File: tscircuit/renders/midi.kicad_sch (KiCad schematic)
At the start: 8 parts, among them U6 H11L1

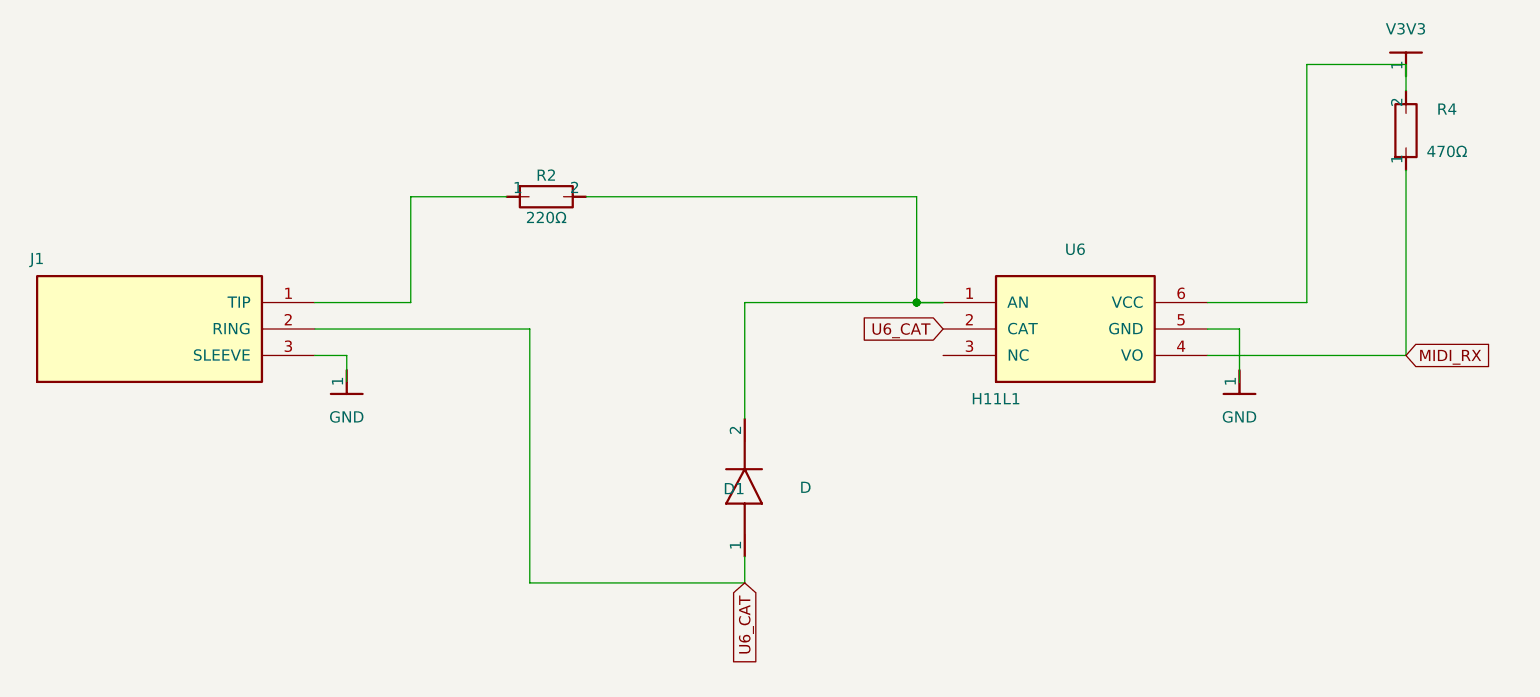
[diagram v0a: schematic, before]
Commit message: tscircuit: full-board schematic-as-code (MIDI + USB + MCU)
Recreate the entire OpenRB rev 0.2 board as tscircuit code from RECONSTRUCTION.md,
using the exact LCSC parts (imported with EasyEDA footprints). Three sheets joined
by shared net-label names; each renders a schematic and exports a native .kicad_sch
that kicad-cli re-opens.

- midi.tsx (§5): DIN-5 MIDI IN -> H11L1 opto (fully hand-wired).
- usb.tsx (§4): USB-C + USBLC6 ESD + CH334R hub + dual USB-A + bulk caps.
- mcu.tsx (§3/§6): RP2040 + power (F1/RT9080) + QSPI flash + 12MHz + reset/boot +
  SWD/UART headers + status LEDs + decoupling.

Independently verified connection-by-connection against RECONSTRUCTION §3-6: all
pass. Fixed one error found in review: C10/C11 100nF moved from +3V3 to the 1.1V
core rail (V1V1) per §2. MIDI connector corrected TRS -> DIN-5.

See REVIEW.md for what to check and the open items (real DIN-5 part, layout tuning).
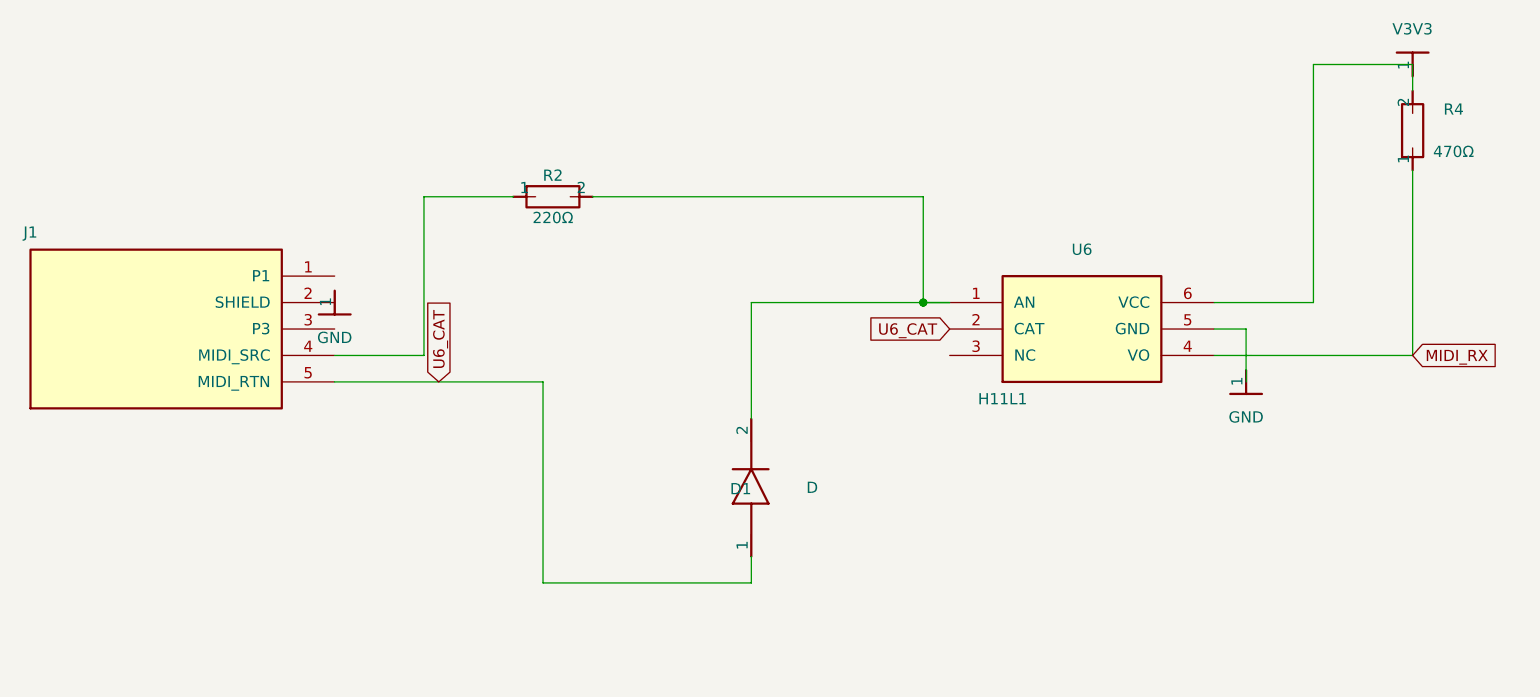
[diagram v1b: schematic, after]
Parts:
- removed GND (x2): GND, symbol Custom:rail_down
- removed J1: (no value), symbol Device:U_chip_pinrow3
- added GND (x2): GND, symbol Custom:rail_down
- added J1: (no value), symbol Device:U_chip_pinrow5
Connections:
- net U6_CAT: now also J1.5 (MIDI_RTN)
- net at R2.1: now also J1.4 (MIDI_SRC)
